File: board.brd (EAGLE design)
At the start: 83.5 x 103.2 mm, 43 parts, among them IC3 MCP23008/SO, J11 AUDIO_JACK_TRRSSMD_RA, J13 AUDIO_JACK_TRRSSMD_RA, J2 455-1750-1-ND, J3 AUDIO_JACK_TRRSSMD_RA, J4 AUDIO_JACK_TRRSSMD_RA, J8 XF2E-2015-1, J9 MOLEX_INC_105027-0001MOLEX_IN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

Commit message: pcb fixes
-added an option for the LCD backlight to be adjusted in the device menu
-changed the sd card slot, now its possible to run the device without an sd card
-changed the case filename - the case probably has to be updated due to the new sd card slot
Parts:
- removed J9: MOLEX_INC_105027-0001MOLEX_INC_105027-0001_0_0, Molex Inc - 105027-0001:MOLEX_INC_105027-0001_0
- removed R4: 100, rcl:R0805
- added C5: 10u, rcl:C0805
- added R3: 100, rcl:R0805
- added SD1: TF-HOLDER, sd-mmc:TF-PULL
- moved C2 9.16 mm to (11.0, 101.6), turned to 0 degrees
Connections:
- new net CARD: J12.6, SD1.9
- new net LED: J12.8, R3.1
- net 3V3: now also SD1.4; no longer J9.P4
- net GND: now also C5.2, J15.12, SD1.6; no longer J12.6, J9.P6
- net N$1: now also R3.2; no longer R4.2
- net SD_CLK: now also SD1.5; no longer J9.P5
- net SD_CMD: now also SD1.3; no longer J9.P3
- net SD_DAT0: now also SD1.7; no longer J9.P7
- net SD_DAT1: now also SD1.8; no longer J9.P8
- net SD_DAT2: now also SD1.1; no longer J9.P1
- net SD_DAT3: now also SD1.2; no longer J9.P2
- net VCC: now also C5.1; no longer R4.1
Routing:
- net LED: track 0.00 -> 37.2 mm, vias 0 -> 2
- net CARD: track 0.00 -> 33.0 mm, vias 0 -> 2
- net SD_DAT2: track 16.4 -> 5.20 mm
- net SD_DAT3: track 14.3 -> 3.45 mm
- net SD_CMD: track 13.7 -> 2.85 mm
- net SD_CLK: track 13.6 -> 2.71 mm
- net SD_DAT0: track 13.4 -> 2.82 mm
- net SD_DAT1: track 12.8 -> 3.41 mm
- net 3V3: track 234.3 -> 230.7 mm
- net N$1: track 5.93 -> 8.47 mm
- net VCC: track 149.7 -> 150.5 mm

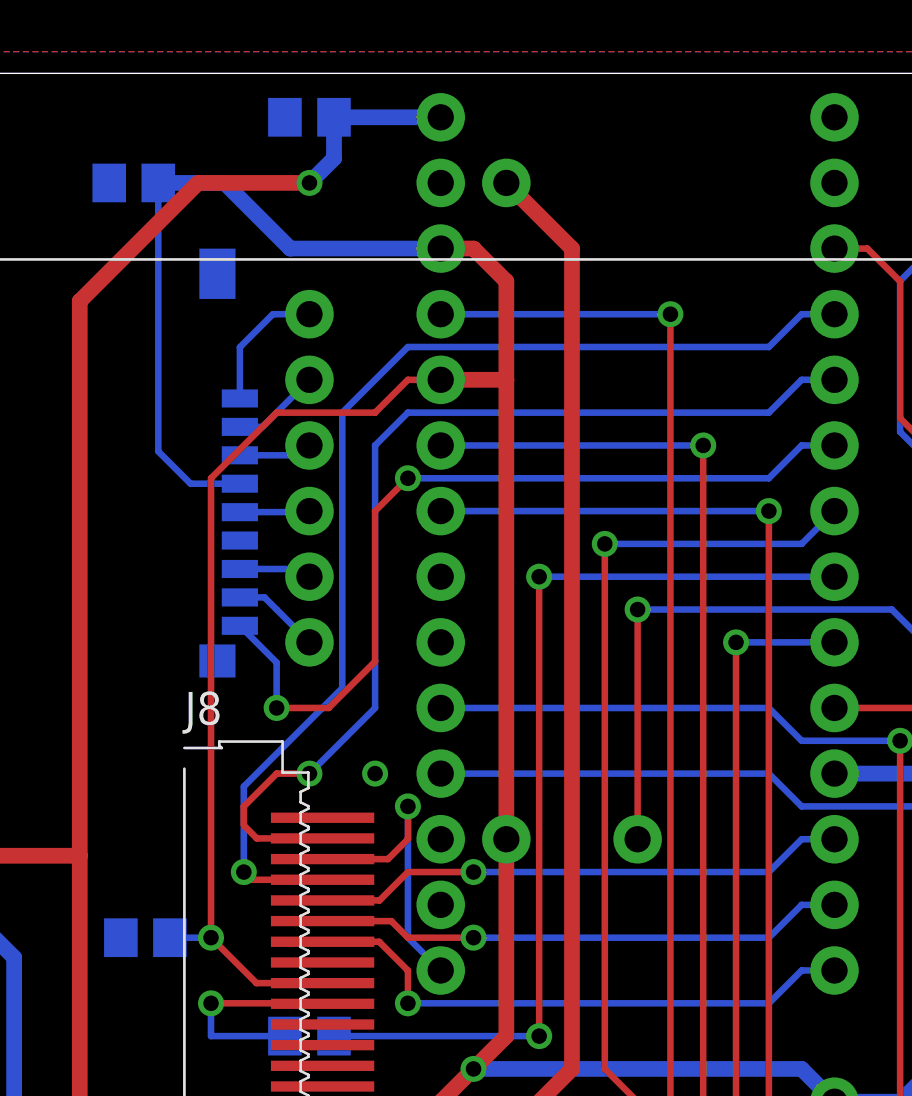
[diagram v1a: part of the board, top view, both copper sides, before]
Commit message: small pcb fix
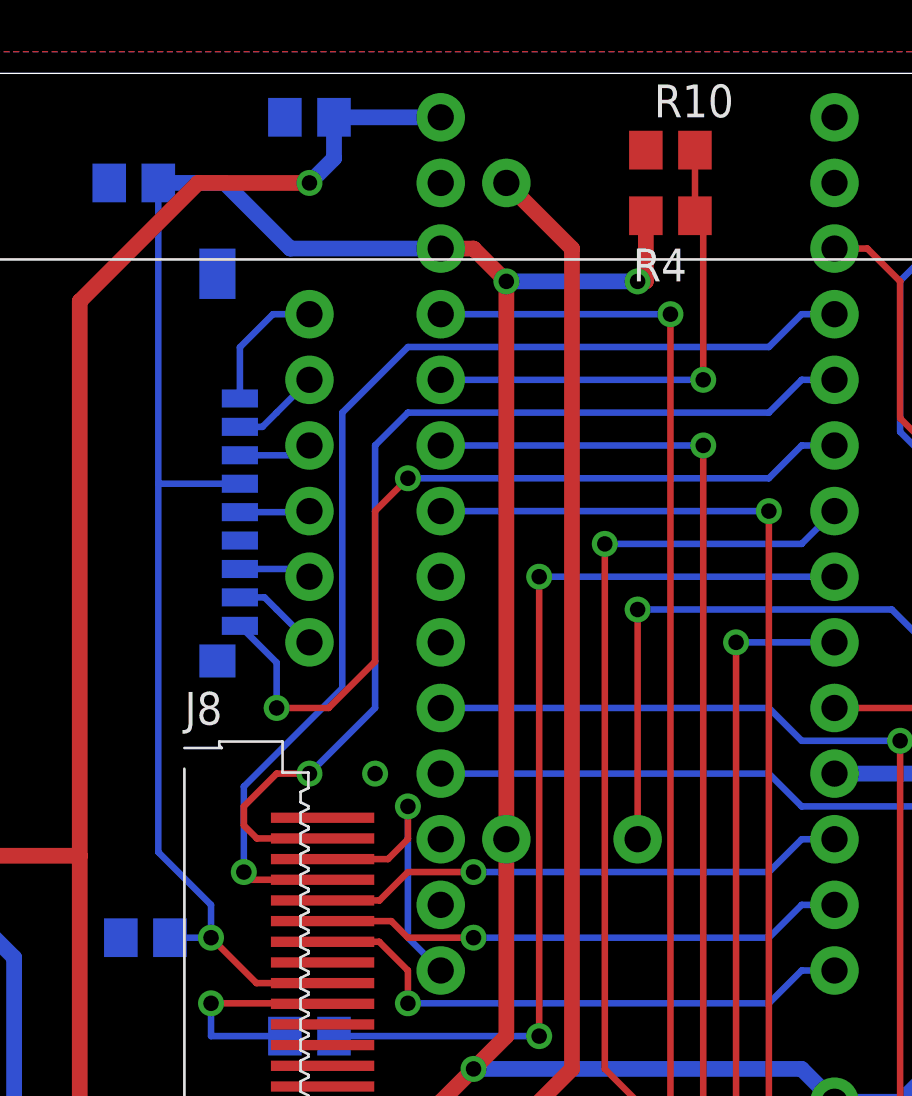
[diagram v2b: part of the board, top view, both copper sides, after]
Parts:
- added R10, R4: 10k, rcl:R0805
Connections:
- new net DIV: J15.5, R10.2, R4.1
- net 3V3: now also R4.2; no longer J15.5
- net GND: now also R10.1
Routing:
- net DIV: track 0.00 -> 19.4 mm, vias 0 -> 1
- net 3V3: track 230.7 -> 227.0 mm, vias 3 -> 5
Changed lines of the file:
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@@
 <element name="R3" library="rcl" package="R0805" value="100" x="17.78" y="68.58" rot="MR0"/>
 <element name="SD1" library="sd-mmc" package="TF-PULL" value="TF-HOLDER" x="7.4676" y="91.059" rot="MR270"/>
+<element name="R4" library="rcl" package="R0805" value="10k" x="31.75" y="100.33" rot="R180"/>
+<element name="R10" library="rcl" package="R0805" value="10k" x="31.75" y="102.87"/>
 </elements>
 <signals>
@@
 <contactref element="J15" pad="12"/>
 <contactref element="SD1" pad="6"/>
+<contactref element="R10" pad="1"/>
 </signal>
 <signal name="VCC">
@@
 <contactref element="J5" pad="1"/>
 <contactref element="J15" pad="3"/>
-<contactref element="J15" pad="5"/>
 <contactref element="IC3" pad="18"/>
 <contactref element="IC3" pad="6"/>
@@
 <wire x1="45.72" y1="71.12" x2="45.72" y2="74.93" width="0.6096" layer="16"/>
 <wire x1="45.72" y1="74.93" x2="45.72" y2="78.74" width="0.6096" layer="16"/>
-<wire x1="22.86" y1="93.98" x2="25.4" y2="93.98" width="0.6096" layer="1"/>
 <wire x1="41.91" y1="81.6" x2="41.91" y2="78.74" width="0.6096" layer="16"/>
 <wire x1="45.72" y1="78.74" x2="41.91" y2="78.74" width="0.6096" layer="16"/>
-<wire x1="25.4" y1="93.98" x2="25.4" y2="76.2" width="0.6096" layer="1"/>
+<wire x1="25.4" y1="97.79" x2="25.4" y2="76.2" width="0.6096" layer="1"/>
 <wire x1="25.4" y1="76.2" x2="25.4" y2="68.58" width="0.6096" layer="1"/>
 <wire x1="25.4" y1="68.58" x2="24.13" y2="67.31" width="0.6096" layer="1"/>
@@
 <wire x1="22.86" y1="99.06" x2="24.13" y2="99.06" width="0.6096" layer="1"/>
 <wire x1="24.13" y1="99.06" x2="25.4" y2="97.79" width="0.6096" layer="1"/>
-<wire x1="25.4" y1="97.79" x2="25.4" y2="93.98" width="0.6096" layer="1"/>
 <contactref element="R1" pad="2"/>
 <contactref element="R2" pad="2"/>
@@
 <wire x1="36.83" y1="67.31" x2="24.13" y2="67.31" width="0.6096" layer="16"/>
 <via x="24.13" y="67.31" extent="1-16" drill="0.6"/>
-<wire x1="20.32" y1="92.71" x2="21.59" y2="93.98" width="0.254" layer="1"/>
-<wire x1="21.59" y1="93.98" x2="22.86" y2="93.98" width="0.254" layer="1"/>
 <contactref element="R6" pad="1"/>
 <wire x1="45.72" y1="78.74" x2="45.72" y2="80.75395" width="0.6096" layer="1"/>
@@
 <wire x1="14.49605" y1="101.6" x2="17.03605" y2="99.06" width="0.6096" layer="16"/>
 <wire x1="17.03605" y1="99.06" x2="22.86" y2="99.06" width="0.6096" layer="16"/>
-<wire x1="15.0876" y1="89.959" x2="13.180903125" y2="89.959" width="0.254" layer="16"/>
-<wire x1="13.180903125" y1="89.959" x2="11.93" y2="91.209903125" width="0.254" layer="16"/>
-<wire x1="11.93" y1="91.209903125" x2="11.93" y2="101.6" width="0.254" layer="16"/>
-<wire x1="20.32" y1="92.71" x2="16.51" y2="92.71" width="0.254" layer="1"/>
-<wire x1="16.51" y1="92.71" x2="13.97" y2="90.17" width="0.254" layer="1"/>
-<wire x1="13.97" y1="90.17" x2="13.97" y2="72.39" width="0.254" layer="1"/>
+<contactref element="R4" pad="2"/>
+<wire x1="13.97" y1="72.39" x2="13.97" y2="73.66" width="0.254" layer="16"/>
+<wire x1="13.97" y1="73.66" x2="11.93" y2="75.7" width="0.254" layer="16"/>
+<wire x1="11.93" y1="75.7" x2="11.93" y2="89.959" width="0.254" layer="16"/>
+<wire x1="11.93" y1="89.959" x2="11.93" y2="101.6" width="0.254" layer="16"/>
+<wire x1="15.0876" y1="89.959" x2="11.93" y2="89.959" width="0.254" layer="16"/>
+<via x="25.4" y="97.79" extent="1-16" drill="0.6"/>
+<wire x1="25.4" y1="97.79" x2="30.48" y2="97.79" width="0.6096" layer="16"/>
+<via x="30.48" y="97.79" extent="1-16" drill="0.6"/>
+<wire x1="30.48" y1="97.79" x2="30.8" y2="97.79" width="0.6096" layer="1"/>
+<wire x1="30.8" y1="97.79" x2="30.8" y2="100.33" width="0.6096" layer="1"/>
 </signal>
 <signal name="D_U">
@@
 <wire x1="18.52395" y1="81.28" x2="16.51" y2="81.28" width="0.254" layer="1"/>
 </signal>
+<signal name="DIV">
+<contactref element="J15" pad="5"/>
+<contactref element="R4" pad="1"/>
+<contactref element="R10" pad="2"/>
+<wire x1="22.86" y1="93.98" x2="33.02" y2="93.98" width="0.254" layer="16"/>
+<via x="33.02" y="93.98" extent="1-16" drill="0.6"/>
+<wire x1="32.7" y1="100.33" x2="33.02" y2="100.33" width="0.254" layer="1"/>
+<wire x1="33.02" y1="100.33" x2="33.02" y2="93.98" width="0.254" layer="1"/>
+<wire x1="32.7" y1="100.33" x2="32.7" y2="102.87" width="0.254" layer="1"/>
+</signal>
 </signals>

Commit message: pcb update
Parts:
- removed R10, R4: 10k, rcl:R0805
- removed R3: 100, rcl:R0805
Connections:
- removed net DIV: J15.5, R10.2, R4.1
- removed net N$1: J8.11, R3.2
- net 3V3: now also J15.5; no longer R4.2
- net GND: no longer R10.1
- net LED: now also J8.11; no longer R3.1
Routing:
- net DIV: track 19.4 -> 0.00 mm, vias 1 -> 0
- net LED: track 37.2 -> 47.5 mm, vias 2 -> 3
- net N$1: track 8.47 -> 0.00 mm, vias 1 -> 0
- net 3V3: track 227.0 -> 221.6 mm, vias 5 -> 4
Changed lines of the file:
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@@
 <element name="C1" library="rcl" package="C0805" value="100n" x="11.43" y="72.39" rot="MR0"/>
 <element name="C5" library="rcl" package="C0805" value="10u" x="17.78" y="104.14" rot="MR0"/>
-<element name="R3" library="rcl" package="R0805" value="100" x="17.78" y="68.58" rot="MR0"/>
 <element name="SD1" library="sd-mmc" package="TF-PULL" value="TF-HOLDER" x="7.4676" y="91.059" rot="MR270"/>
-<element name="R4" library="rcl" package="R0805" value="10k" x="31.75" y="100.33" rot="R180"/>
-<element name="R10" library="rcl" package="R0805" value="10k" x="31.75" y="102.87"/>
 </elements>
 <signals>
@@
 <contactref element="J15" pad="12"/>
 <contactref element="SD1" pad="6"/>
-<contactref element="R10" pad="1"/>
 </signal>
 <signal name="VCC">
@@
 <wire x1="41.91" y1="81.6" x2="41.91" y2="78.74" width="0.6096" layer="16"/>
 <wire x1="45.72" y1="78.74" x2="41.91" y2="78.74" width="0.6096" layer="16"/>
-<wire x1="25.4" y1="97.79" x2="25.4" y2="76.2" width="0.6096" layer="1"/>
+<wire x1="25.4" y1="97.79" x2="25.4" y2="93.98" width="0.6096" layer="1"/>
+<wire x1="25.4" y1="93.98" x2="25.4" y2="76.2" width="0.6096" layer="1"/>
 <wire x1="25.4" y1="76.2" x2="25.4" y2="68.58" width="0.6096" layer="1"/>
 <wire x1="25.4" y1="68.58" x2="24.13" y2="67.31" width="0.6096" layer="1"/>
@@
 <wire x1="14.49605" y1="101.6" x2="17.03605" y2="99.06" width="0.6096" layer="16"/>
 <wire x1="17.03605" y1="99.06" x2="22.86" y2="99.06" width="0.6096" layer="16"/>
-<contactref element="R4" pad="2"/>
 <wire x1="13.97" y1="72.39" x2="13.97" y2="73.66" width="0.254" layer="16"/>
 <wire x1="13.97" y1="73.66" x2="11.93" y2="75.7" width="0.254" layer="16"/>
@@
 <wire x1="11.93" y1="89.959" x2="11.93" y2="101.6" width="0.254" layer="16"/>
 <wire x1="15.0876" y1="89.959" x2="11.93" y2="89.959" width="0.254" layer="16"/>
-<via x="25.4" y="97.79" extent="1-16" drill="0.6"/>
-<wire x1="25.4" y1="97.79" x2="30.48" y2="97.79" width="0.6096" layer="16"/>
-<via x="30.48" y="97.79" extent="1-16" drill="0.6"/>
-<wire x1="30.48" y1="97.79" x2="30.8" y2="97.79" width="0.6096" layer="1"/>
-<wire x1="30.8" y1="97.79" x2="30.8" y2="100.33" width="0.6096" layer="1"/>
+<contactref element="J15" pad="5"/>
+<wire x1="22.86" y1="93.98" x2="25.4" y2="93.98" width="0.6096" layer="16"/>
+<via x="25.4" y="93.98" extent="1-16" drill="0.6"/>
 </signal>
 <signal name="D_U">
@@
 <wire x1="26.67" y1="86.36" x2="26.67" y2="68.58" width="0.254" layer="1"/>
 <via x="26.67" y="68.58" extent="1-16" drill="0.6"/>
-<contactref element="R3" pad="1"/>
-<wire x1="18.73" y1="68.58" x2="26.67" y2="68.58" width="0.254" layer="16"/>
+<contactref element="J8" pad="11"/>
+<wire x1="26.67" y1="68.58" x2="13.97" y2="68.58" width="0.254" layer="16"/>
+<wire x1="13.97" y1="68.58" x2="13.97" y2="69.85" width="0.254" layer="16"/>
+<via x="13.97" y="69.85" extent="1-16" drill="0.6"/>
+<wire x1="13.97" y1="69.85" x2="18.288" y2="69.85" width="0.254" layer="1"/>
+<wire x1="18.288" y1="69.85" x2="18.288" y2="69.831" width="0.254" layer="1"/>
 </signal>
 <signal name="N$2">
@@
 <wire x1="20.32" y1="81.28" x2="17.78" y2="78.74" width="0.254" layer="16"/>
 </signal>
-<signal name="N$1">
-<contactref element="J8" pad="11"/>
-<contactref element="R3" pad="2"/>
-<wire x1="16.83" y1="68.58" x2="13.97" y2="68.58" width="0.254" layer="16"/>
-<wire x1="13.97" y1="68.58" x2="13.97" y2="69.85" width="0.254" layer="16"/>
-<via x="13.97" y="69.85" extent="1-16" drill="0.6"/>
-<wire x1="13.97" y1="69.85" x2="18.288" y2="69.85" width="0.254" layer="1"/>
-<wire x1="18.288" y1="69.85" x2="18.288" y2="69.831" width="0.254" layer="1"/>
-</signal>
 <signal name="CARD">
 <contactref element="J12" pad="6"/>
@@
 <wire x1="18.52395" y1="81.28" x2="16.51" y2="81.28" width="0.254" layer="1"/>
 </signal>
-<signal name="DIV">
-<contactref element="J15" pad="5"/>
-<contactref element="R4" pad="1"/>
-<contactref element="R10" pad="2"/>
-<wire x1="22.86" y1="93.98" x2="33.02" y2="93.98" width="0.254" layer="16"/>
-<via x="33.02" y="93.98" extent="1-16" drill="0.6"/>
-<wire x1="32.7" y1="100.33" x2="33.02" y2="100.33" width="0.254" layer="1"/>
-<wire x1="33.02" y1="100.33" x2="33.02" y2="93.98" width="0.254" layer="1"/>
-<wire x1="32.7" y1="100.33" x2="32.7" y2="102.87" width="0.254" layer="1"/>
-</signal>
 </signals>
